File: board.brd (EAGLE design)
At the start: 50 x 50 mm, 27 parts

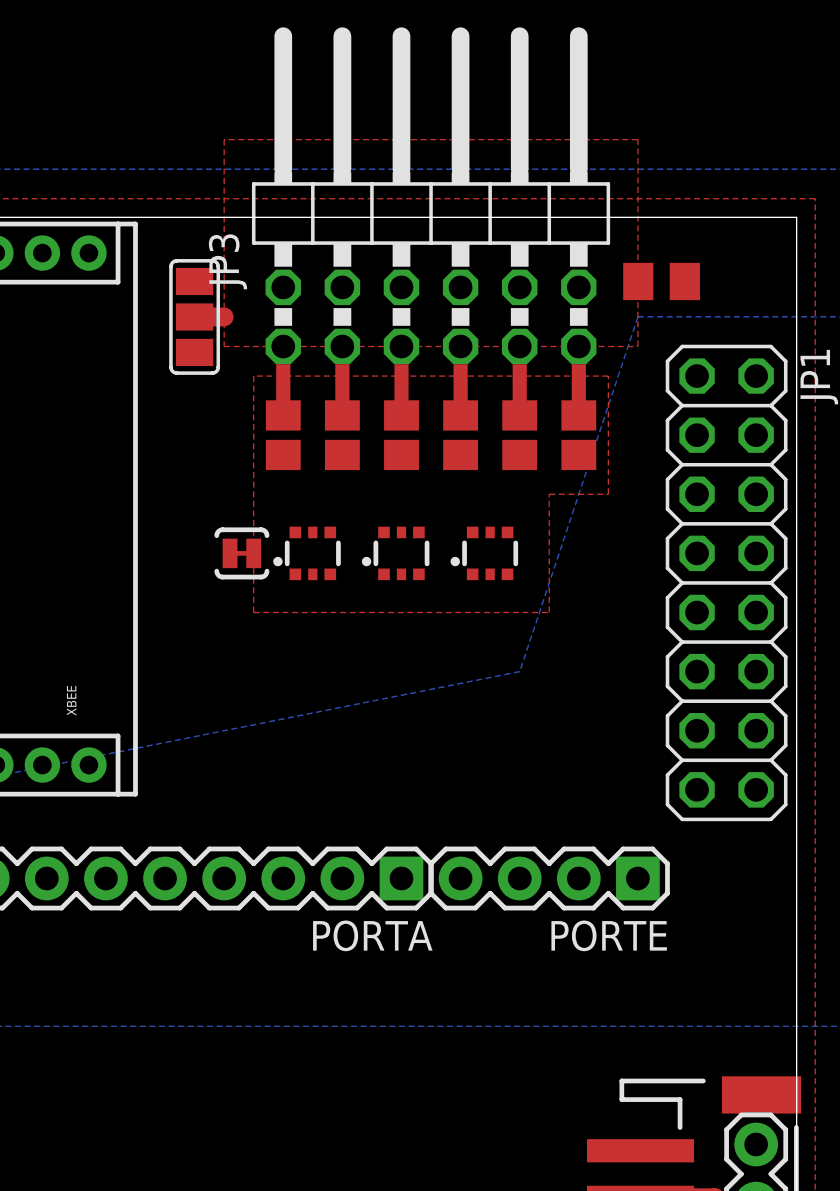
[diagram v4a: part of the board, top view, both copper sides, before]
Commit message: bigger cap for the leds
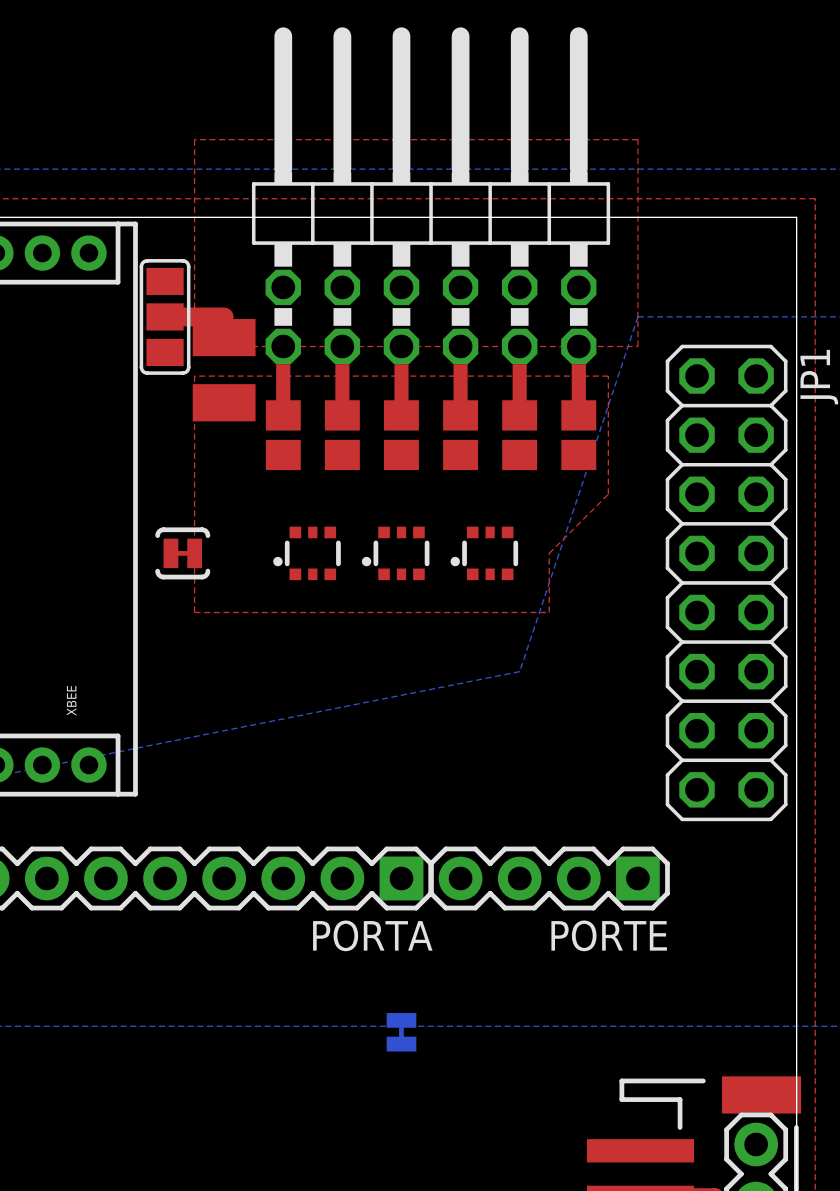
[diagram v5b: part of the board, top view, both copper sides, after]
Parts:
- removed C2: (no value), resistor:C0805K
- removed SJ1: SOLDERJUMPERTRACE, SparkFun-Passives:SJ_2S-TRACE
- added AGND_GND, PGND_GND: SOLDERJUMPERTRACE, SparkFun-Passives:SJ_2S-TRACE
- added C3: (no value), rcl:C1210
- moved SJ2 1.27 mm to (22.9, 45.7)
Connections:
- removed net GND_PWR: DRV0.1, DRV0.4, DRV1.1, DRV1.4, DRV2.1, DRV2.4, SJ1.2
- new net PGND: C3.2, DRV0.1, DRV0.4, DRV1.1, DRV1.4, DRV2.1, DRV2.4, PGND_GND.2
- net AGND: now also AGND_GND.1
- net GND: now also AGND_GND.2, PGND_GND.1; no longer C2.2, SJ1.1
- net VLED: now also C3.1; no longer C2.1
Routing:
- net VLED: track 1.27 -> 2.54 mm
- added copper zone on layer 1, net PGND
- removed copper zone on layer 1, net GND_PWR
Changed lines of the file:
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@@
 <element name="C1" library="rcl" package="C0603K" value="0.1uF" x="8.89" y="24.13" smashed="yes" rot="MR0"/>
 <element name="JP1" library="pinhead" package="2X08" value="" x="46.99" y="34.29" rot="R270"/>
-<element name="SJ2" library="SparkFun-Passives" package="SJ_2" value="" x="24.13" y="45.72" smashed="yes" rot="R270">
-<attribute name="VALUE" x="24.13" y="45.8201" size="0.02" layer="27" rot="R270"/>
+<element name="SJ2" library="SparkFun-Passives" package="SJ_2" value="" x="22.86" y="45.72" smashed="yes" rot="R270">
+<attribute name="VALUE" x="22.86" y="45.8201" size="0.02" layer="27" rot="R270"/>
 </element>
 <element name="RLED0" library="resistor" package="R0805" value="" x="27.94" y="40.64" smashed="yes" rot="R90">
@@
 <attribute name="VALUE" x="42.926" y="39.878" size="1.27" layer="27" rot="R90"/>
 </element>
-<element name="C2" library="resistor" package="C0805K" value="" x="44.196" y="47.244" smashed="yes">
-<attribute name="VALUE" x="43.196" y="45.344" size="1.016" layer="27"/>
-</element>
-<element name="SJ1" library="SparkFun-Passives" package="SJ_2S-TRACE" value="SOLDERJUMPERTRACE" x="26.162" y="35.56" smashed="yes"/>
-<element name="JP3" library="pinhead" package="2X06/90" value="" x="34.29" y="50.8"/>
+<element name="PGND_GND" library="SparkFun-Passives" package="SJ_2S-TRACE" value="SOLDERJUMPERTRACE" x="23.622" y="35.56" smashed="yes"/>
+<element name="JP3" library="pinhead" package="2X06/90" value="" x="34.29" y="50.8" smashed="yes">
+<attribute name="VALUE" x="43.815" y="46.99" size="1.27" layer="27" rot="R90"/>
+</element>
+<element name="AGND_GND" library="SparkFun-Passives" package="SJ_2S-TRACE" value="SOLDERJUMPERTRACE" x="33.02" y="14.986" smashed="yes" rot="MR270"/>
+<element name="C3" library="rcl" package="C1210" value="" x="25.4" y="43.434" smashed="yes" rot="R270">
+<attribute name="VALUE" x="22.225" y="45.339" size="1.27" layer="27" rot="R270"/>
+</element>
 </elements>
 <signals>
@@
 <via x="10.16" y="36.83" extent="1-16" drill="0.3048"/>
 <via x="8.89" y="36.83" extent="1-16" drill="0.3048"/>
-<contactref element="C2" pad="2"/>
-<contactref element="SJ1" pad="1"/>
+<contactref element="PGND_GND" pad="1"/>
+<contactref element="AGND_GND" pad="2"/>
 </signal>
 <signal name="PDI_DATA">
@@
 <contactref element="PORTC" pad="7"/>
 </signal>
-<signal name="GND_PWR" class="1">
+<signal name="PGND" class="1">
 <contactref element="DRV0" pad="1"/>
 <contactref element="DRV0" pad="4"/>
@@
 <contactref element="DRV1" pad="1"/>
 <polygon width="0.4064" layer="1" isolate="0.254" rank="5">
-<vertex x="26.67" y="43.18"/>
-<vertex x="26.67" y="33.02"/>
+<vertex x="24.13" y="43.18"/>
+<vertex x="24.13" y="33.02"/>
 <vertex x="39.37" y="33.02"/>
-<vertex x="39.37" y="38.1"/>
+<vertex x="39.37" y="35.56"/>
 <vertex x="41.91" y="38.1"/>
 <vertex x="41.91" y="43.18"/>
 </polygon>
-<contactref element="SJ1" pad="2"/>
+<contactref element="PGND_GND" pad="2"/>
+<contactref element="C3" pad="2"/>
 </signal>
 <signal name="PWM0">
@@
 <wire x1="46.482" y1="7.874" x2="43.306" y2="7.874" width="0.8128" layer="1"/>
 <wire x1="43.306" y1="7.874" x2="43.29" y2="7.89" width="0.8128" layer="1"/>
-<wire x1="7.62" y1="16.83" x2="24.13" y2="47.244" width="0" layer="19" extent="1-16"/>
+<wire x1="7.62" y1="16.83" x2="22.86" y2="47.244" width="0" layer="19" extent="1-16"/>
 <wire x1="43.29" y1="7.89" x2="7.62" y2="16.83" width="0" layer="19" extent="1-16"/>
 </signal>
@@
 <vertex x="53.34" y="15.24"/>
 </polygon>
+<contactref element="AGND_GND" pad="1"/>
 </signal>
 <signal name="PA0">
@@
 <signal name="VLED">
 <polygon width="0.4064" layer="1" isolate="0.254" rank="5">
-<vertex x="25.4" y="53.34"/>
-<vertex x="25.4" y="44.45"/>
+<vertex x="24.13" y="53.34"/>
+<vertex x="24.13" y="44.45"/>
 <vertex x="43.18" y="44.45"/>
 <vertex x="43.18" y="53.34"/>
 </polygon>
 <contactref element="SJ2" pad="2"/>
-<wire x1="24.13" y1="45.72" x2="25.4" y2="45.72" width="0.8128" layer="1"/>
-<contactref element="C2" pad="1"/>
+<wire x1="22.86" y1="45.72" x2="25.4" y2="45.72" width="0.8128" layer="1"/>
 <contactref element="JP3" pad="2"/>
 <contactref element="JP3" pad="4"/>
@@
 <contactref element="JP3" pad="10"/>
 <contactref element="JP3" pad="12"/>
+<contactref element="C3" pad="1"/>
 </signal>
 <signal name="LED1" class="1">
@@
 <contactref element="SJ2" pad="3"/>
 <contactref element="XBEE" pad="1"/>
-<wire x1="1.59" y1="26.465" x2="24.13" y2="44.196" width="0" layer="19" extent="1-1"/>
+<wire x1="1.59" y1="26.465" x2="22.86" y2="44.196" width="0" layer="19" extent="1-1"/>
 </signal>
 <signal name="LED0R" class="1">

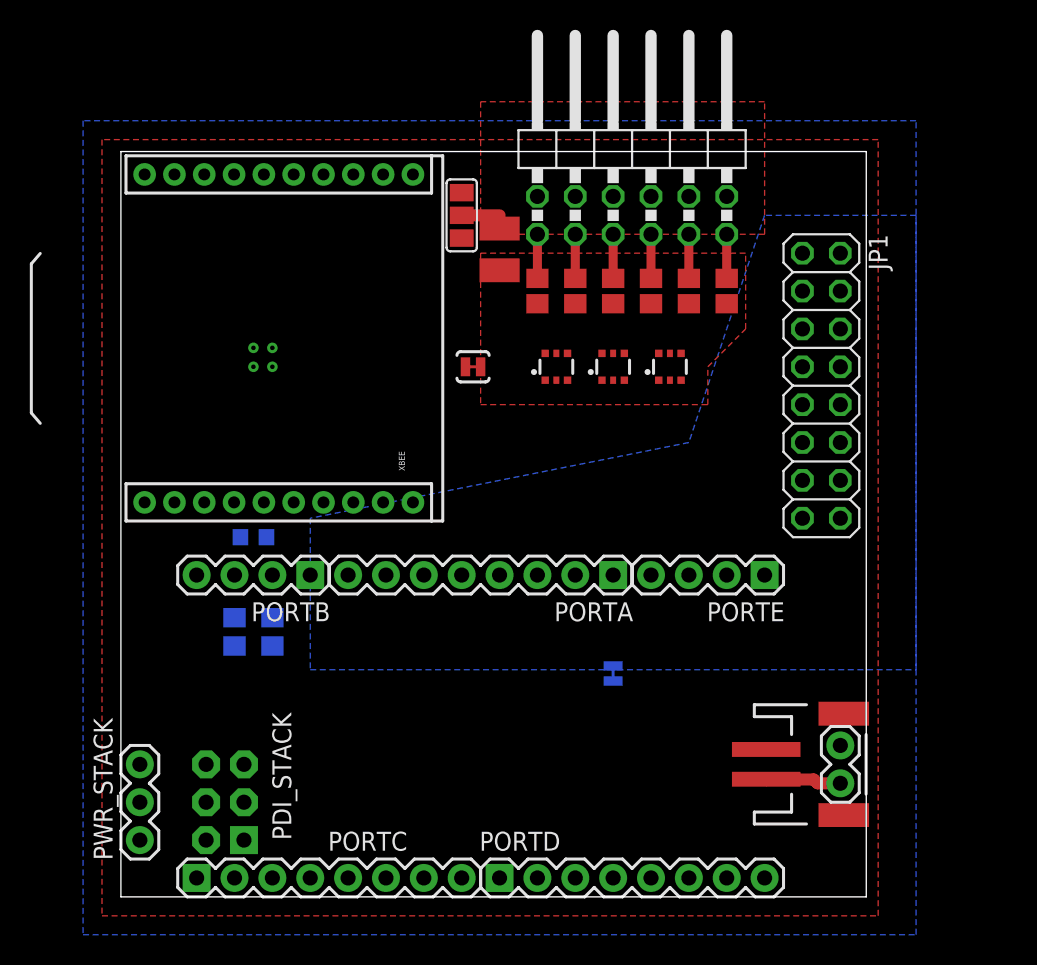
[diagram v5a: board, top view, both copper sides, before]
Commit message: xbee and xmega share aref
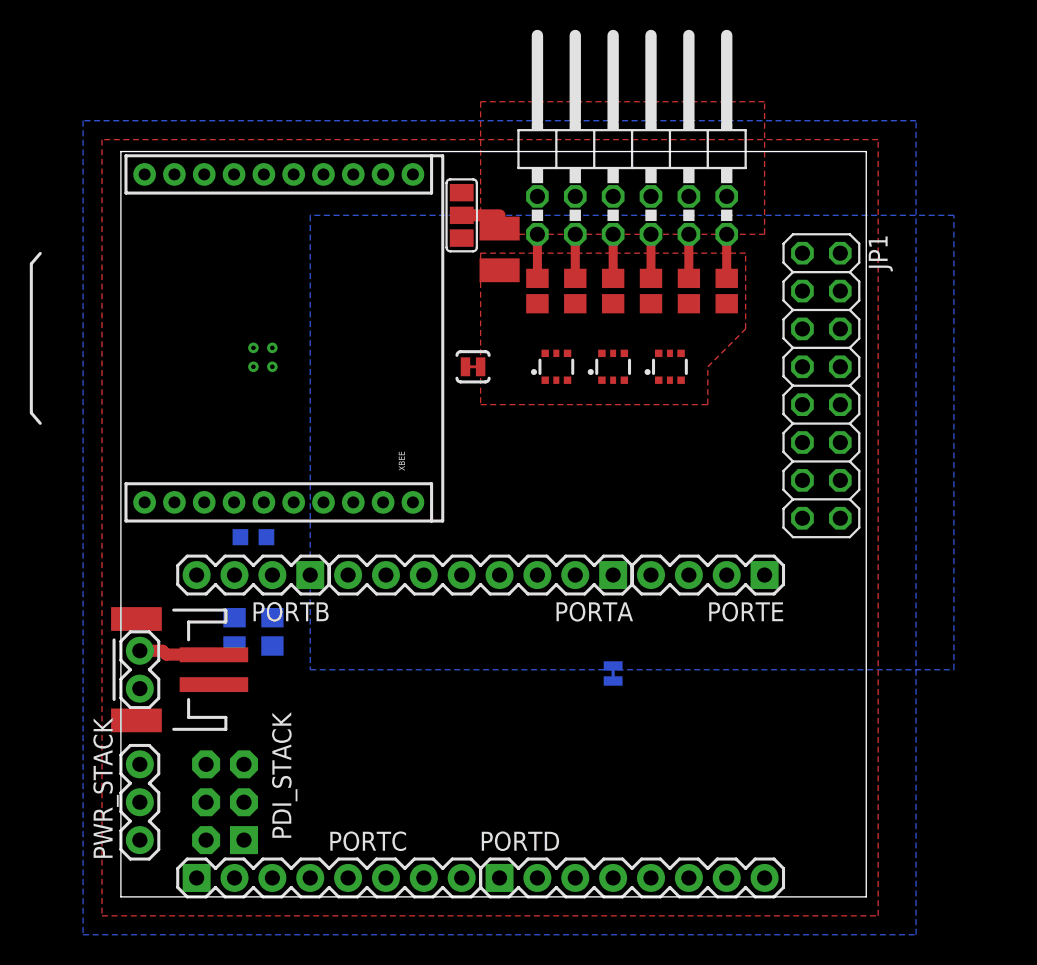
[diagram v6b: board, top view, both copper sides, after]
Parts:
- moved BAT_ALT 47.1 mm to (1.27, 14.0), turned to 90 degrees
- moved BAT 44.9 mm to (2.54, 15.2), turned to 90 degrees
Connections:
- new net PB0/XMEGA_AREF: PORTB.1, XBEE.14
- new net XBEE_RESET: PORTD.5, XBEE.5
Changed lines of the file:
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@@
 <attribute name="VALUE" x="38.481" y="35.052" size="0.4064" layer="27" ratio="10"/>
 </element>
-<element name="BAT" library="SparkFun-Connectors" package="JST-2-SMD" value="" x="46.99" y="8.89" smashed="yes" rot="R270">
-<attribute name="PROD_ID" value="CONN-08352" x="46.99" y="8.89" size="1.778" layer="27" rot="R270" display="off"/>
-<attribute name="VALUE" x="46.99" y="10.16" size="0.4064" layer="27" rot="R270"/>
-</element>
-<element name="BAT_ALT" library="SparkFun-Connectors" package="1X02" value="" x="48.26" y="10.16" smashed="yes" rot="R270">
-<attribute name="VALUE" x="45.085" y="11.43" size="1.27" layer="27" rot="R270"/>
+<element name="BAT" library="SparkFun-Connectors" package="JST-2-SMD" value="" x="2.54" y="15.24" smashed="yes" rot="R90">
+<attribute name="PROD_ID" value="CONN-08352" x="2.54" y="15.24" size="1.778" layer="27" rot="R90" display="off"/>
+<attribute name="VALUE" x="2.54" y="13.97" size="0.4064" layer="27" rot="R90"/>
+</element>
+<element name="BAT_ALT" library="SparkFun-Connectors" package="1X02" value="" x="1.27" y="13.97" smashed="yes" rot="R90">
+<attribute name="VALUE" x="4.445" y="12.7" size="1.27" layer="27" rot="R90"/>
 </element>
 <element name="R1" library="rcl" package="R0805" value="100k" x="7.62" y="17.78" smashed="yes" rot="MR270">
@@
 <contactref element="BAT" pad="2"/>
 <contactref element="BAT_ALT" pad="2"/>
-<wire x1="43.29" y1="7.62" x2="43.29" y2="7.89" width="0.4064" layer="1"/>
+<wire x1="6.24" y1="16.51" x2="6.24" y2="16.24" width="0.4064" layer="1"/>
 <contactref element="R1" pad="2"/>
 <contactref element="SJ2" pad="1"/>
-<wire x1="48.26" y1="7.62" x2="46.736" y2="7.62" width="0.8128" layer="1"/>
-<wire x1="46.736" y1="7.62" x2="46.482" y2="7.874" width="0.8128" layer="1"/>
-<wire x1="46.482" y1="7.874" x2="43.306" y2="7.874" width="0.8128" layer="1"/>
-<wire x1="43.306" y1="7.874" x2="43.29" y2="7.89" width="0.8128" layer="1"/>
+<wire x1="1.27" y1="16.51" x2="2.794" y2="16.51" width="0.8128" layer="1"/>
+<wire x1="2.794" y1="16.51" x2="3.048" y2="16.256" width="0.8128" layer="1"/>
+<wire x1="3.048" y1="16.256" x2="6.224" y2="16.256" width="0.8128" layer="1"/>
+<wire x1="6.224" y1="16.256" x2="6.24" y2="16.24" width="0.8128" layer="1"/>
 <wire x1="7.62" y1="16.83" x2="22.86" y2="47.244" width="0" layer="19" extent="1-16"/>
-<wire x1="43.29" y1="7.89" x2="7.62" y2="16.83" width="0" layer="19" extent="1-16"/>
+<wire x1="6.24" y1="16.51" x2="7.62" y2="16.83" width="0" layer="19" extent="1-16"/>
 </signal>
 <signal name="VBAT_SENSE">
@@
 <contactref element="JP1" pad="14"/>
 <polygon width="0.4064" layer="16" isolate="0.254" rank="5">
-<vertex x="53.34" y="45.72"/>
-<vertex x="43.18" y="45.72"/>
-<vertex x="38.1" y="30.48"/>
-<vertex x="12.7" y="25.4"/>
+<vertex x="55.88" y="45.72"/>
+<vertex x="12.7" y="45.72"/>
 <vertex x="12.7" y="15.24"/>
-<vertex x="53.34" y="15.24"/>
+<vertex x="55.88" y="15.24"/>
 </polygon>
 <contactref element="AGND_GND" pad="1"/>
@@
 <wire x1="33.77" y1="34.66" x2="35.56" y2="39.79" width="0" layer="19" extent="1-1"/>
 </signal>
+<signal name="PB0/XMEGA_AREF">
+<contactref element="PORTB" pad="1"/>
+<contactref element="XBEE" pad="14"/>
+<wire x1="12.7" y1="21.59" x2="13.59" y2="48.465" width="0" layer="19" extent="1-1"/>
+</signal>
+<signal name="XBEE_RESET">
+<contactref element="XBEE" pad="5"/>
+<contactref element="PORTD" pad="5"/>
+<wire x1="9.59" y1="26.465" x2="35.56" y2="1.27" width="0" layer="19" extent="1-1"/>
+</signal>
 </signals>
